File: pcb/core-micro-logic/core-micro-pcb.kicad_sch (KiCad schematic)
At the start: 58 parts, among them J1 Screw_Terminal_01x02, J2 Screw_Terminal_01x02, J3 Screw_Terminal_01x02, J4 Screw_Terminal_01x02, J5 Screw_Terminal_01x02, J6 Screw_Terminal_01x02, J7 USB_C_Receptacle_USB2.0, J8 SWD, J9 HR911105A, SW1 SW_Push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

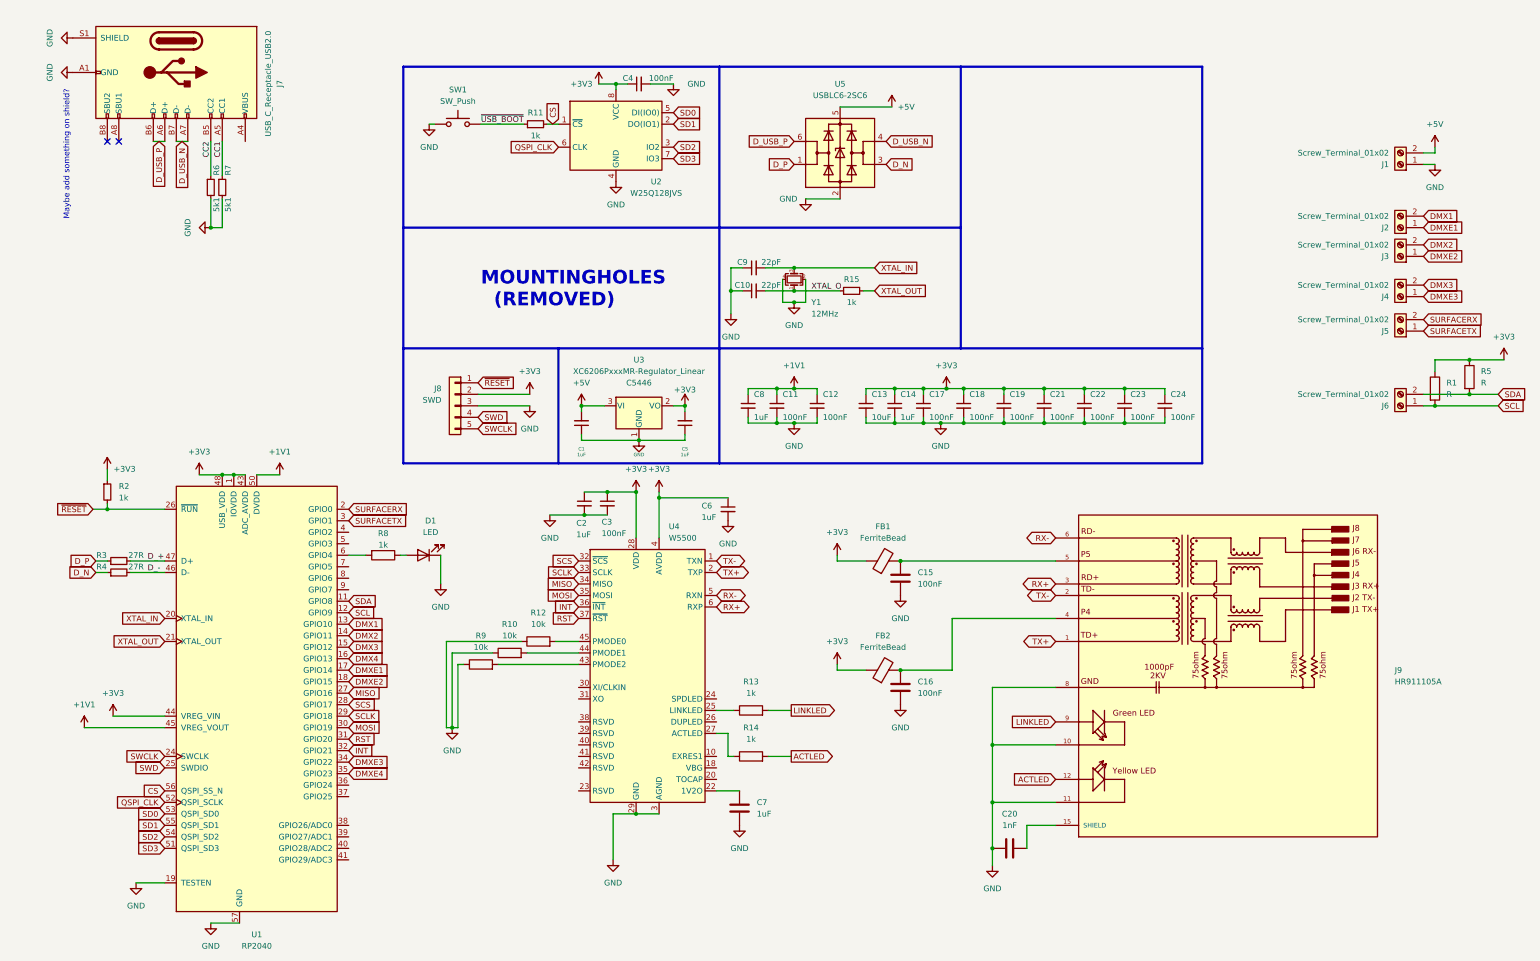
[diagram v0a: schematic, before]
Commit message: masde schematic look nicer
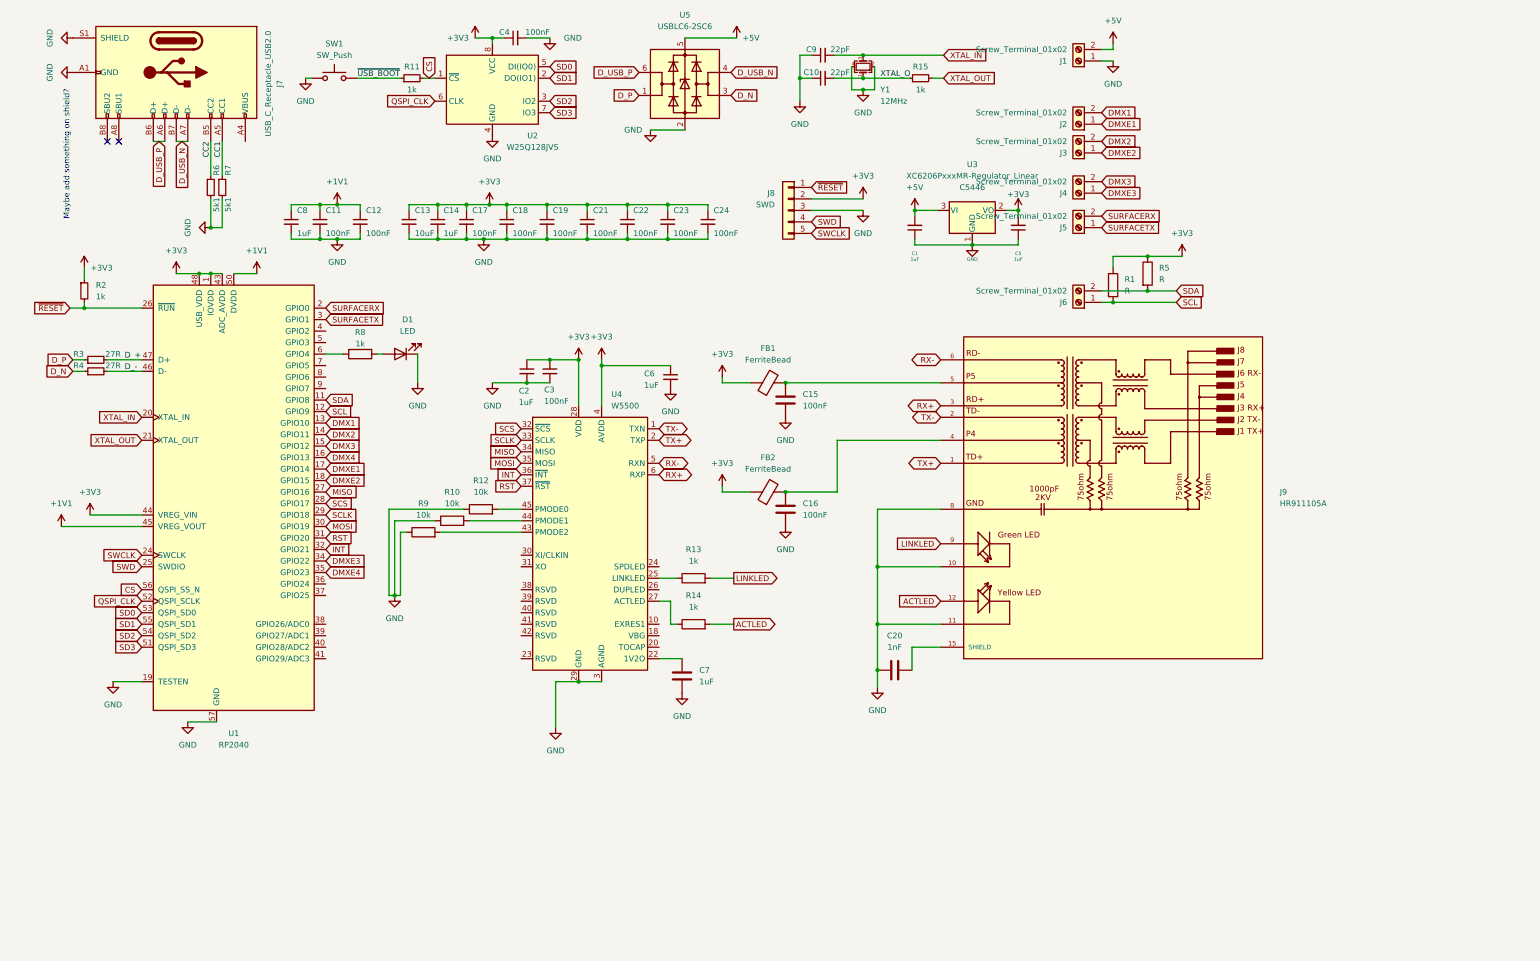
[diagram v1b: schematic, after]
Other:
- note removed: "MOUNTINGHOLES (REMOVED)"
- moved on the sheet: C1, C10, C11, C12, C13, C14, C15, C16, C17, C18, C19, C2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
